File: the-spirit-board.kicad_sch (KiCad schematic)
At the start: 49 parts, among them IC1 ESP32-C6-WROOM-1-N8, IC2 AP2112K-3.3TRG1, J1 RAHUC31AUTR, Q1 BSS138, Q2 BSS138, Q3 BSS138, Q4 BSS138, Q5 BSS138, Q6 BSS138, Q7 BSS138

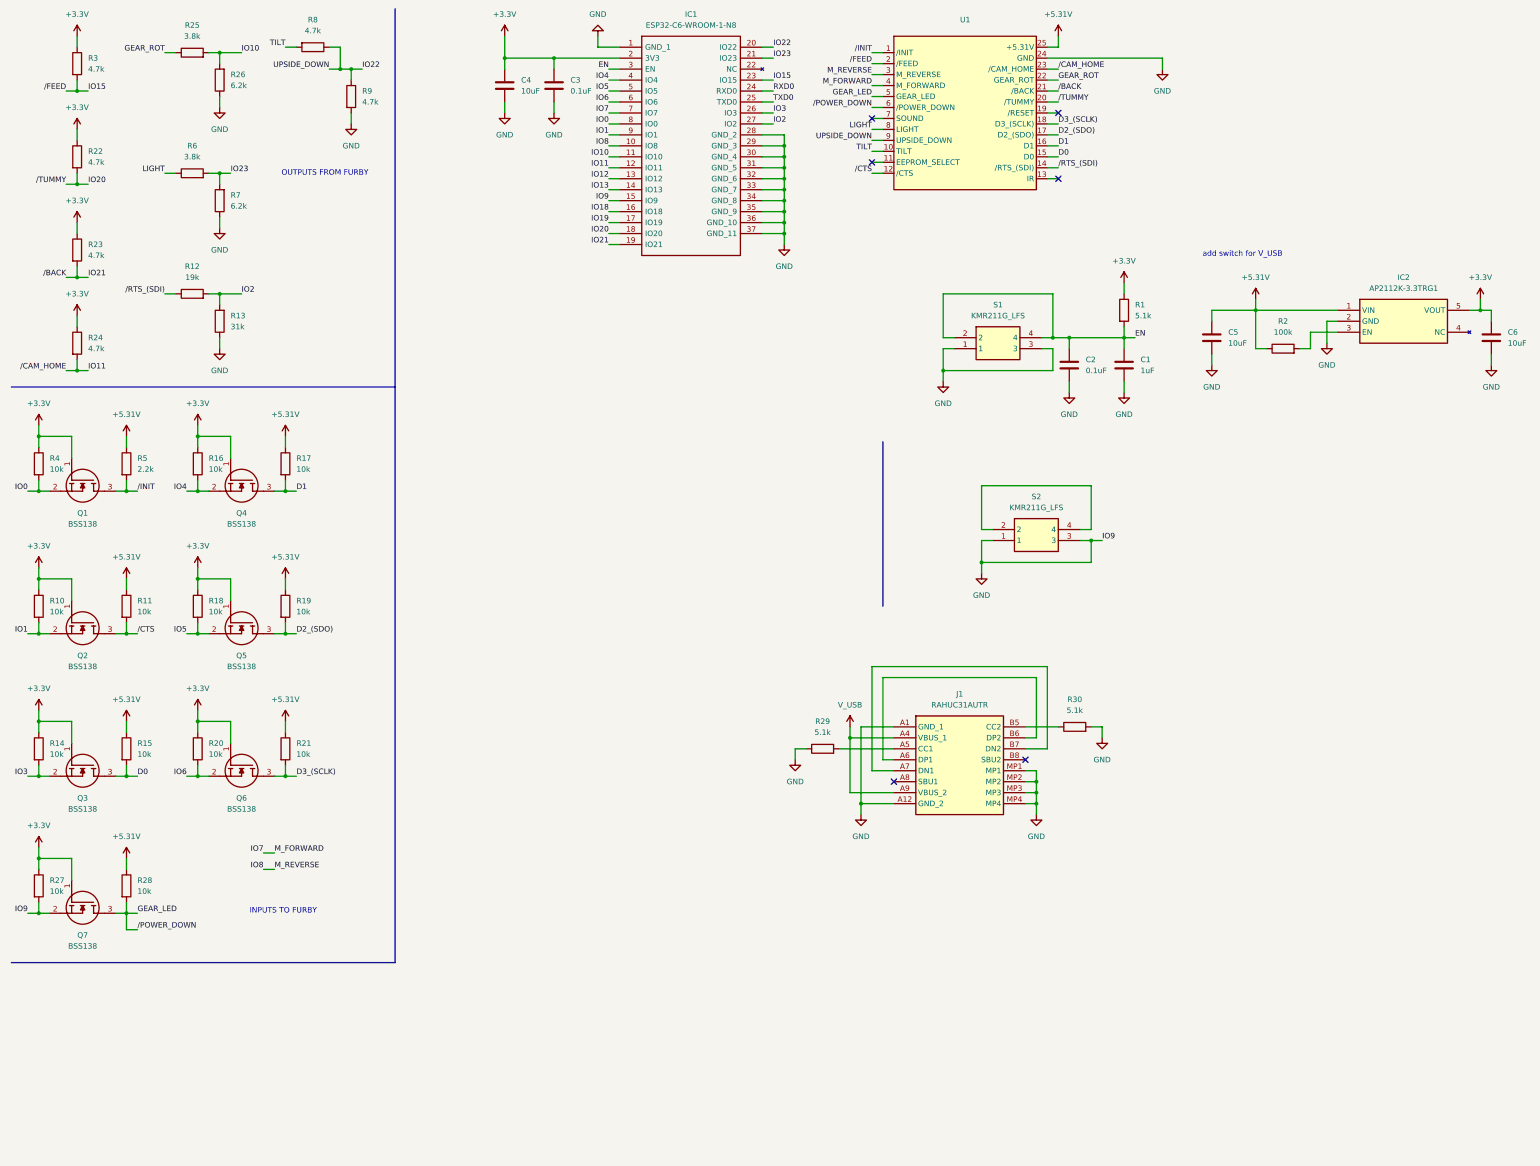
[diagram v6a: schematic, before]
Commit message: Add an I2S microphone module
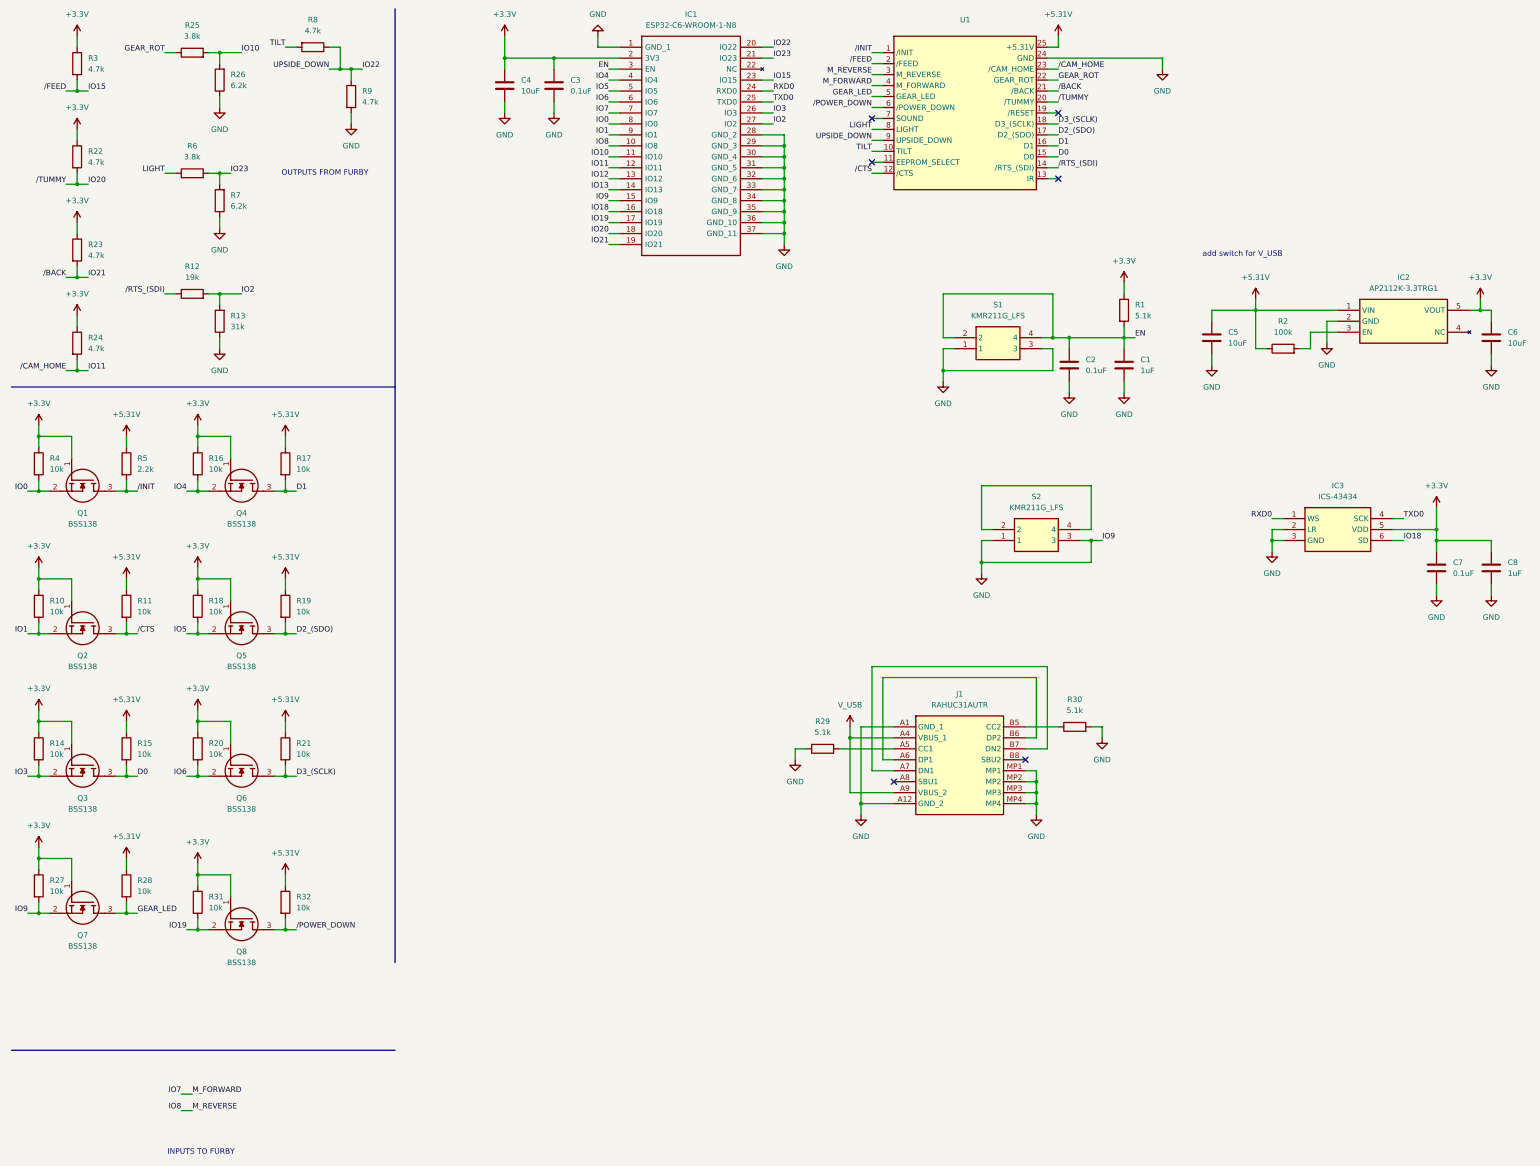
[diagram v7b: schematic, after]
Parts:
- added C7: 0.1uF, Capacitor_SMD:C_0603_1608Metric, symbol Device:C
- added C8: 1uF, Capacitor_SMD:C_0603_1608Metric, symbol Device:C
- added IC3: ICS-43434, ICS43434, symbol TheSPIRITBoard:ICS-43434
- added Q8: BSS138, SOT95P240X120-3N, symbol TheSPIRITBoard:BSS138
- added R31, R32: 10k, Resistor_SMD:R_0603_1608Metric, symbol Device:R
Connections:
- net +3.3V: now also C7.2, C8.2, IC3.5 (VDD), Q8.1 (G), R31.1
- net +5.31V: now also R32.1
- net GEAR_LED: no longer U1.6 (/POWER_DOWN)
- net GND: now also C7.1, C8.1, IC3.2 (LR), IC3.3 (GND)
- net IO18: now also IC3.6 (SD)
- net IO19: now also Q8.2 (S), R31.2
- net RXD0: now also IC3.1 (WS)
- net TXD0: now also IC3.4 (SCK)
- new net /POWER_DOWN: Q8.3 (D), R32.2, U1.6 (/POWER_DOWN)

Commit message: Initial draft of the schematic complete
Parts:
- added D1: B340A-E3/61T, Diode_SMD:D_SMA, symbol Device:D_Schottky
- added D2: LED, LED_SMD:LED_0603_1608Metric, symbol Device:LED
- added Q9: DMG3415U-7, TheSPIRITBoard:SOT96P240X110-3N, symbol TheSPIRITBoard:DMG3415U-7
- added R33: 100k, Resistor_SMD:R_0603_1608Metric, symbol Device:R
- added R34: 5.1k, Resistor_SMD:R_0603_1608Metric, symbol Device:R
- IC1: footprint ESP32C6WROOM1N8 -> TheSPIRITBoard:ESP32C6WROOM1N8
- IC2: footprint SOT95P285X140-5N -> TheSPIRITBoard:SOT95P285X140-5N
- IC3: footprint ICS43434 -> TheSPIRITBoard:ICS43434
- J1: footprint RAHUC31AUTR -> TheSPIRITBoard:RAHUC31AUTR
- Q1, Q2, Q3, Q4, Q5, Q6, Q7, Q8: footprint SOT95P240X120-3N -> TheSPIRITBoard:SOT95P240X120-3N
- S1, S2: footprint KMR_2 -> TheSPIRITBoard:KMR_2
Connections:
- net +5.31V: now also Q9.3 (D); no longer C5.2, IC2.1 (VIN), R2.1
- net GND: now also D2.1 (K), R33.1
- net IO0: now also R34.1
- net IO12: now also J1.A7 (DN1), J1.B7 (DN2)
- net IO13: now also J1.A6 (DP1), J1.B6 (DP2)
- net V_USB: now also D1.2 (A), Q9.1 (G), R33.2
- new net: D2.2 (A), R34.2
- new net: C5.2, D1.1 (K), IC2.1 (VIN), Q9.2 (S), R2.1
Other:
- note added: "BOOT SELECT AND ENABLE"
- note added: "ESP32-C6"
- note added: "FURBY CONNECTOR"
- note added: "I2S MICROPHONE MODULE"
- note added: "LED"
- note added: "POWER SUPPLY"
- note added: "USB-C CONNECTOR"
- note removed: "add switch for V_USB"
- moved on the sheet: C1, C2, C3, C4, C5, C6, C7, C8, IC1, IC2, IC3, J1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
